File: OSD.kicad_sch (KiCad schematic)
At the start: 16 parts, among them U5 MAX7456EUI+, Y2 27MHz

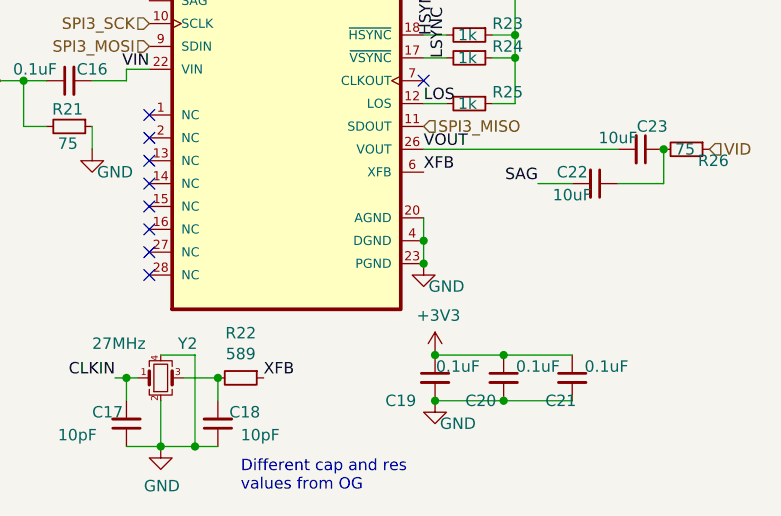
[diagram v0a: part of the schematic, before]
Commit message: Finished power and signal routing.
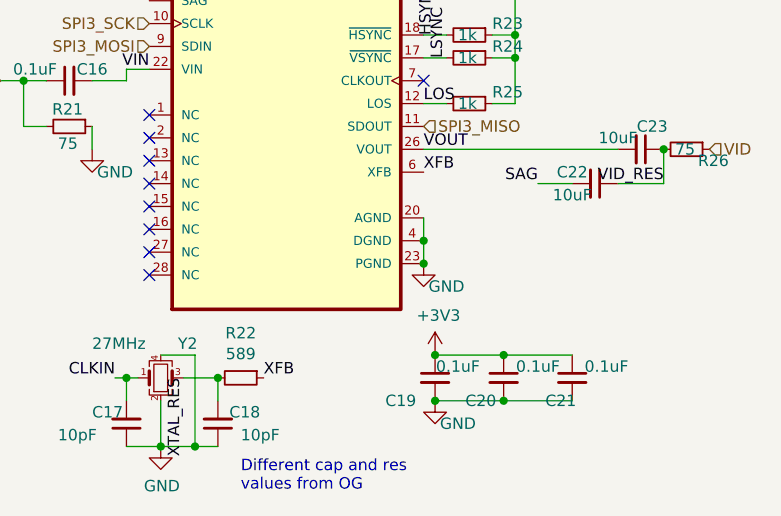
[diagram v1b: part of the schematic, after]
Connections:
- net XTAL_RES: now reaches C18.2, R22.2, Y2.3
- net VID_RES: now reaches C22.1, C23.1, R26.2
